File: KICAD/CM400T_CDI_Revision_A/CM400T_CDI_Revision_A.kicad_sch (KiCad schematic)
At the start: 42 parts, among them P1 Brown, P2 Green Coil, P3 Black w/ White, P4 Yellow Coil, P5 Blue, P6 White, P7 Light Blue, P8 Green Harness, P9 Pink

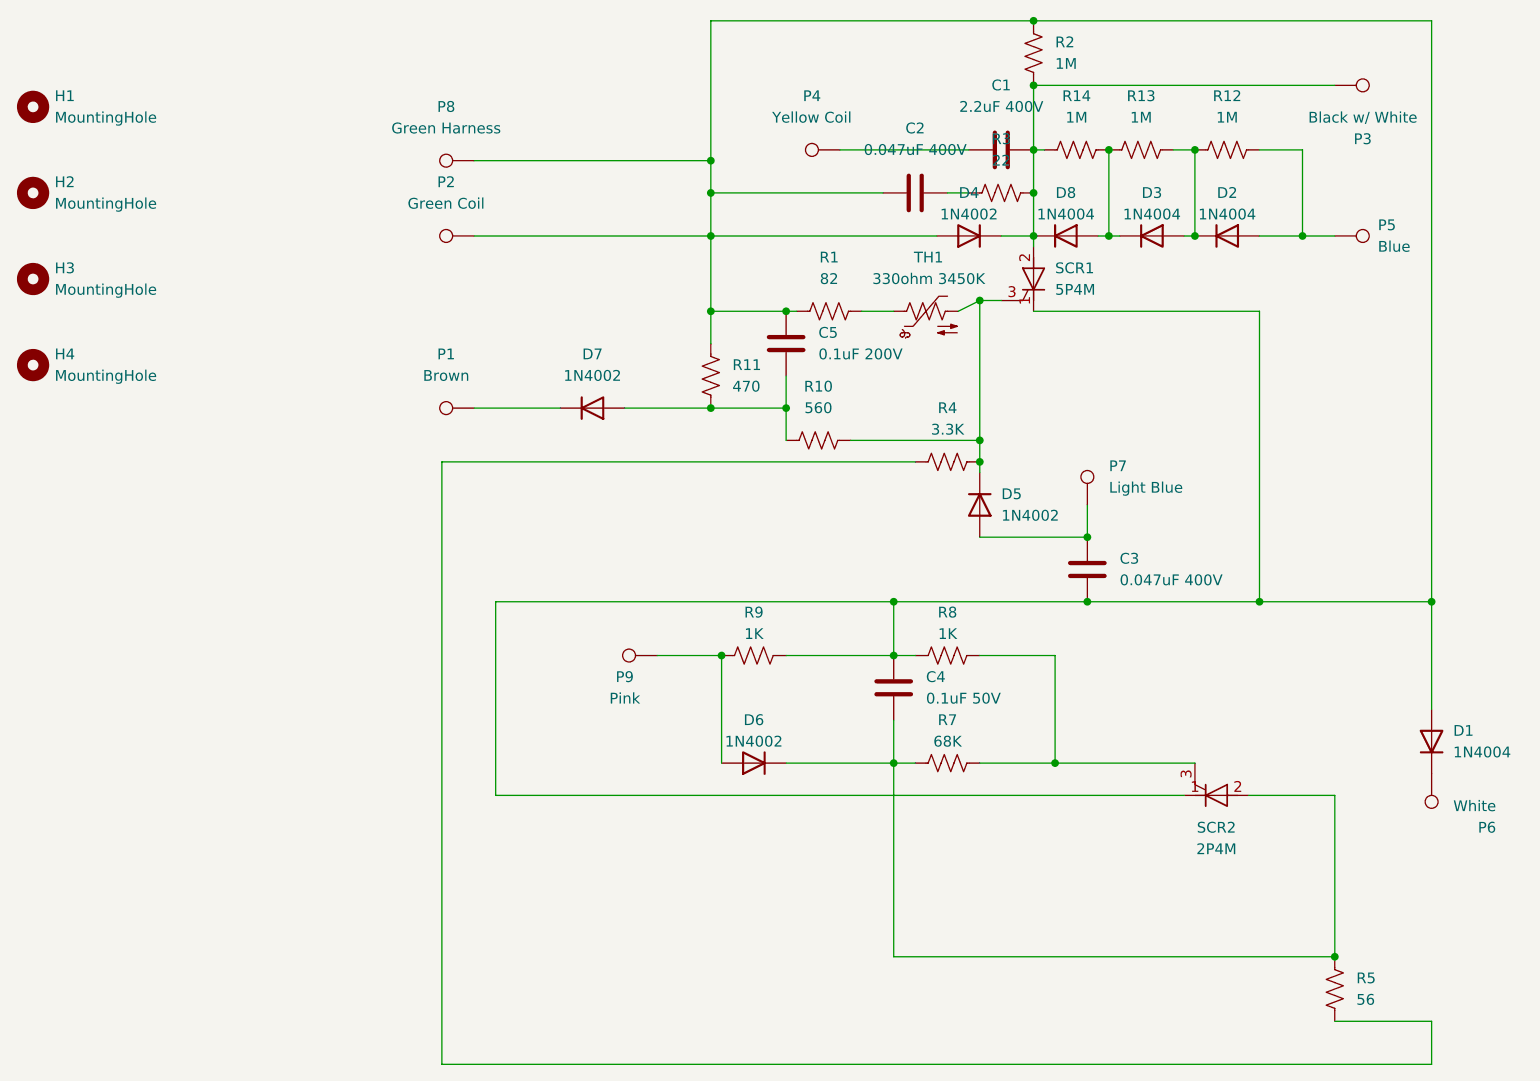
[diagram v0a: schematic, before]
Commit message: make rev a schematic more readable.
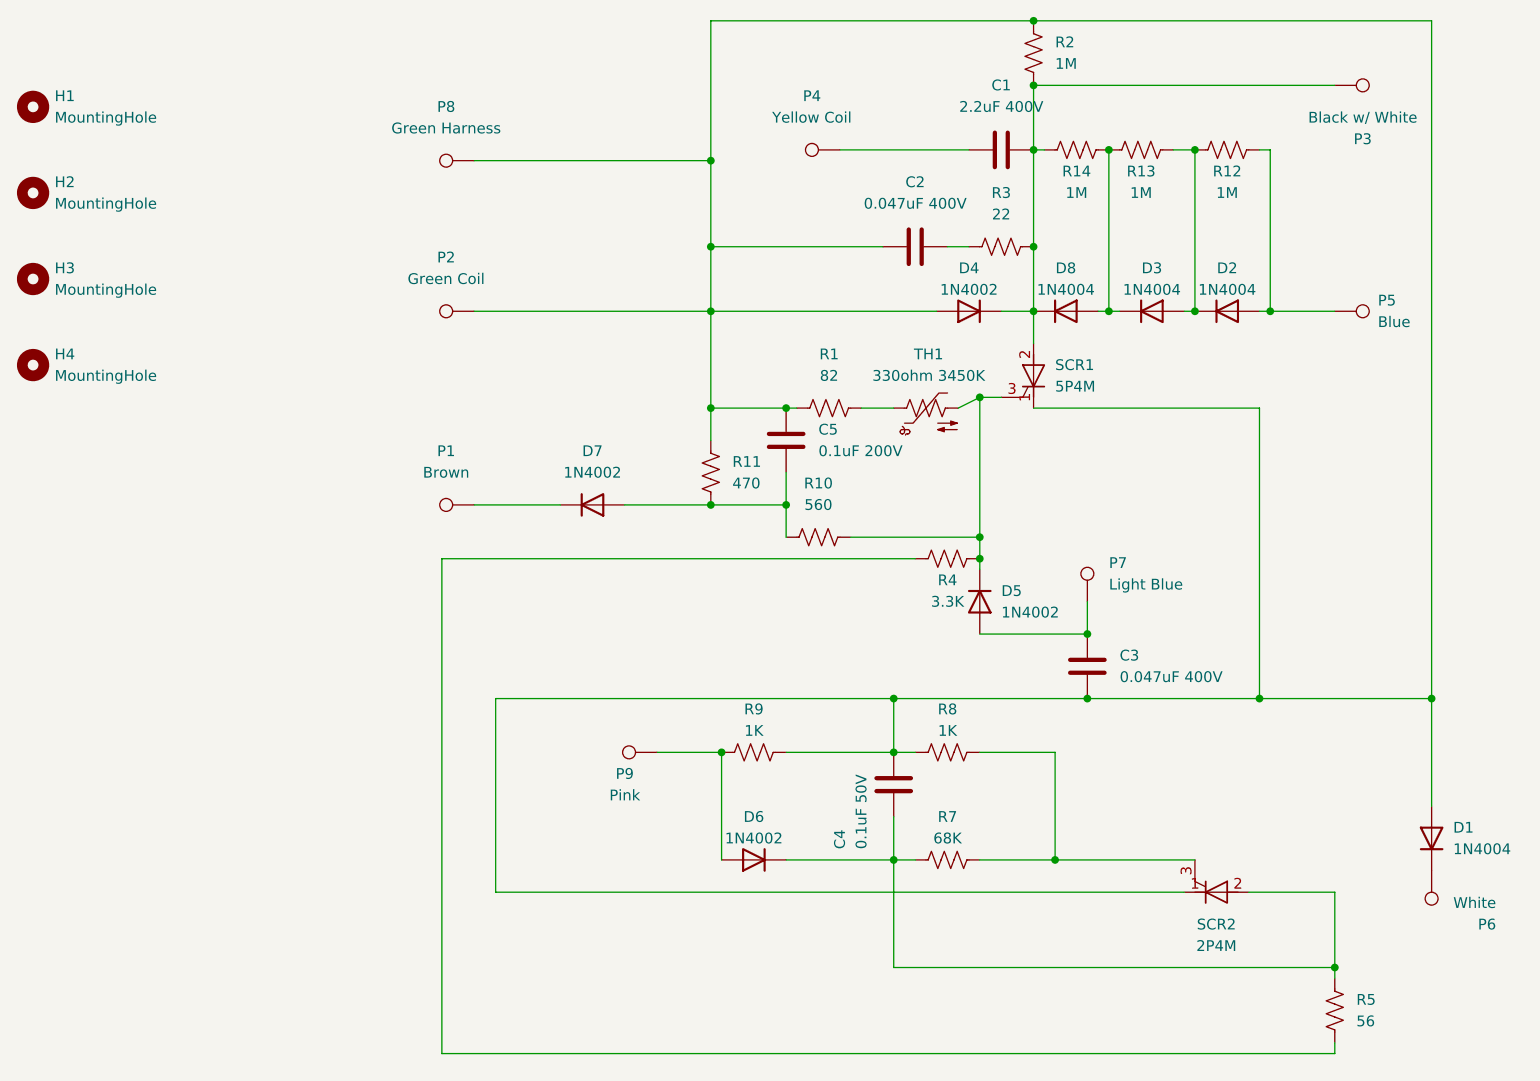
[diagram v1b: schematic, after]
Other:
- moved on the sheet: C2, C3, C4, C5, D1, D2, D3, D4, D5, D6, D7, D8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
